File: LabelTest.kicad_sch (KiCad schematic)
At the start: 0 parts

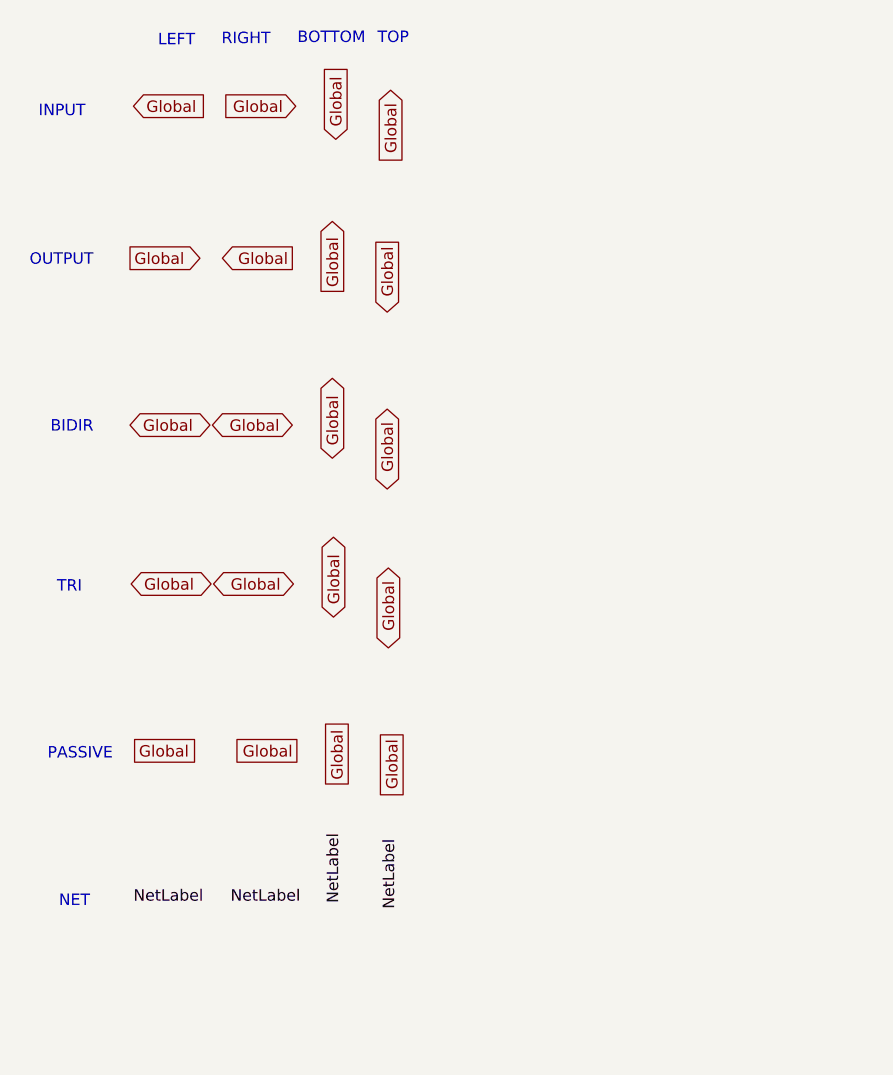
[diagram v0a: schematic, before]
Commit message: add hierarchical labels
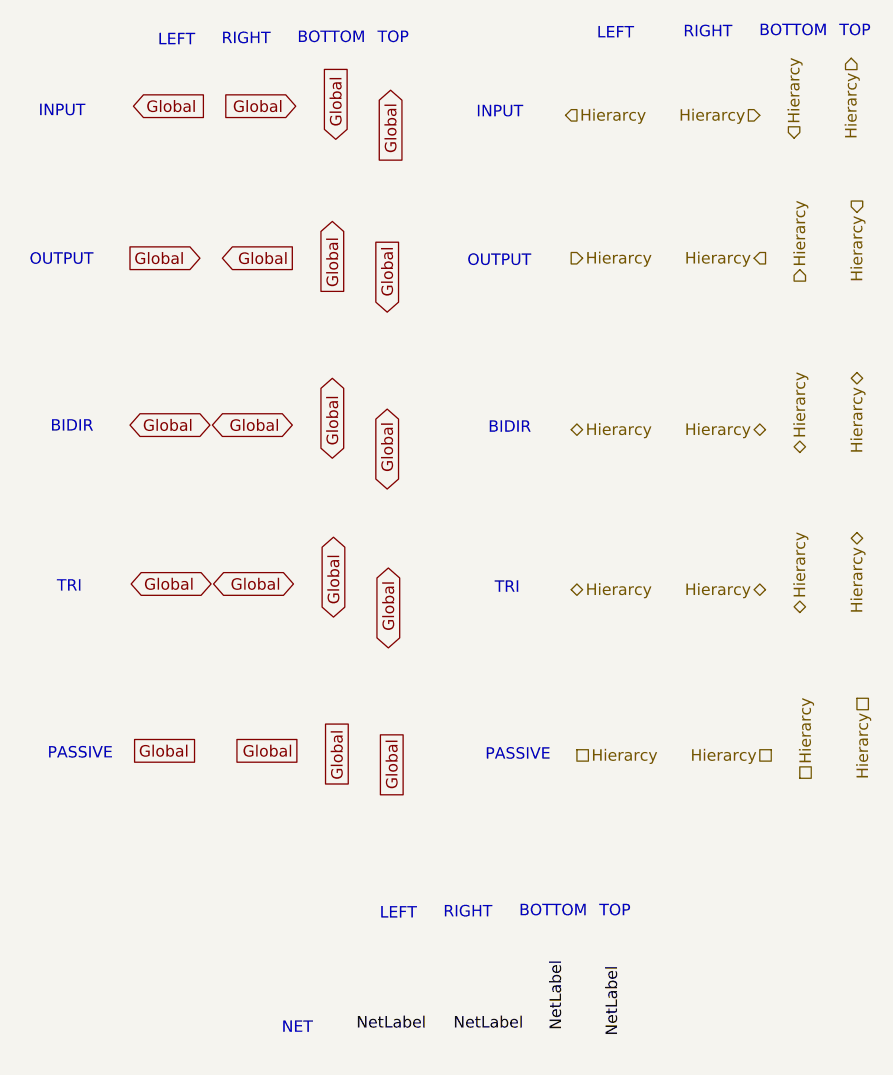
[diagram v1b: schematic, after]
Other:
- company: (none) -> Circuitly, Inc.
- title: (none) -> Global/Net Label orientation tests
